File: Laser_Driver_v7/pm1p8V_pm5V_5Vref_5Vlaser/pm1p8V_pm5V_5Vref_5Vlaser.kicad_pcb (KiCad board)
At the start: 2 copper layers, 160 x 100 mm, 103 parts, among them J6 DIN41612_03x32_C_Split, U1 MC7808CTG, U10 LT3042EMSE +14.3V, U13 MC7812CTG, U14 MC7808CTG, U15 LT3045EMSE 5V, U16 LT3045EMSE 5V, U17 MC7808CTG, U18 MC7906CTG, U19 LT3045EMSE 5V, U2 LT3042EMSE +5.5V, U20 LT3094EMSE -5V, U21 OPA192IDBVR, U3 LTC6655BHMS8-5#PBF, U4 MC7812CTG, U5 MC7805CTG, U6 LT3045EMSE 3.3V, U7 LP5907MFX-1.8, U8 TPS7A3901DSCR, U9 LT3094EMSE -14.3V

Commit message: Working towards a full set of pcbs in v7
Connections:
- J6 pad a20: unconnected-(J6A-Pin_a20-Pada20) -> 5Vref
- J6 pad a22: unconnected-(J6A-Pin_a22-Pada22) -> VREF_MID
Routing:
- net +18V: track 269.0 -> 307.0 mm, vias 0 -> 5
- net +5V_LASER: track 112.0 -> 92.9 mm, vias 1 -> 2
- net 5Vref: track 78.4 -> 96.8 mm
- net +5V: track 138.6 -> 147.9 mm, vias 2 -> 4
- net 1V8: track 71.3 -> 77.4 mm, vias 2 -> 4
- net 3V3: track 84.3 -> 90.3 mm, vias 2 -> 4
- net -15V: track 65.4 -> 70.2 mm, vias 2 -> 4
- net -18V: track 226.3 -> 229.8 mm, vias 1 -> 2
- net -5V: track 146.5 -> 147.8 mm, vias 2 -> 3
- net VREF_MID: track 75.2 -> 75.9 mm, vias 1 -> 2
- net Net-(U10-EN/UV): track 33.5 -> 34.1 mm
- net +15V: track 66.1 -> 66.7 mm, vias 1 -> 3
- net GND: track 51.6 -> 51.7 mm, vias 270 -> 245

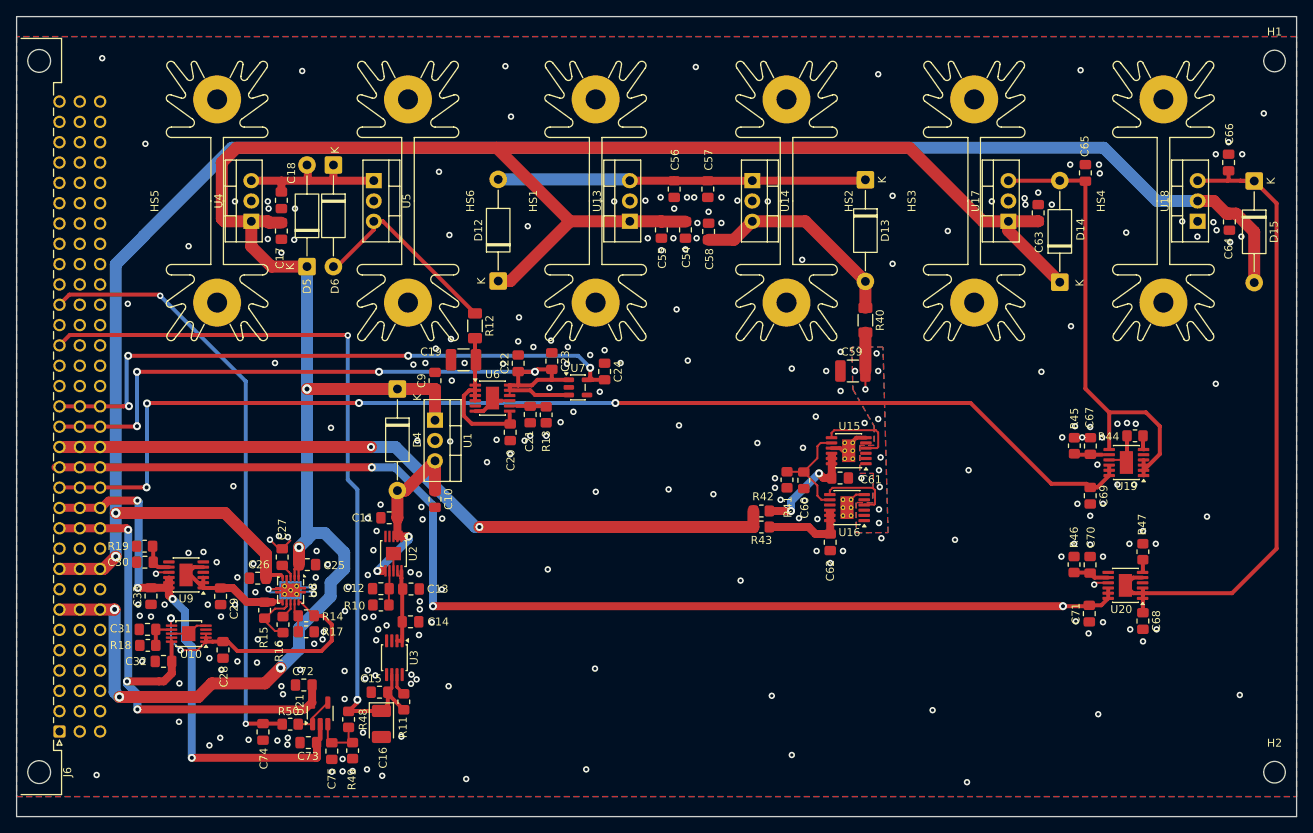
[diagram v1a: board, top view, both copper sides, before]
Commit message: Updates to capacitors for derating.
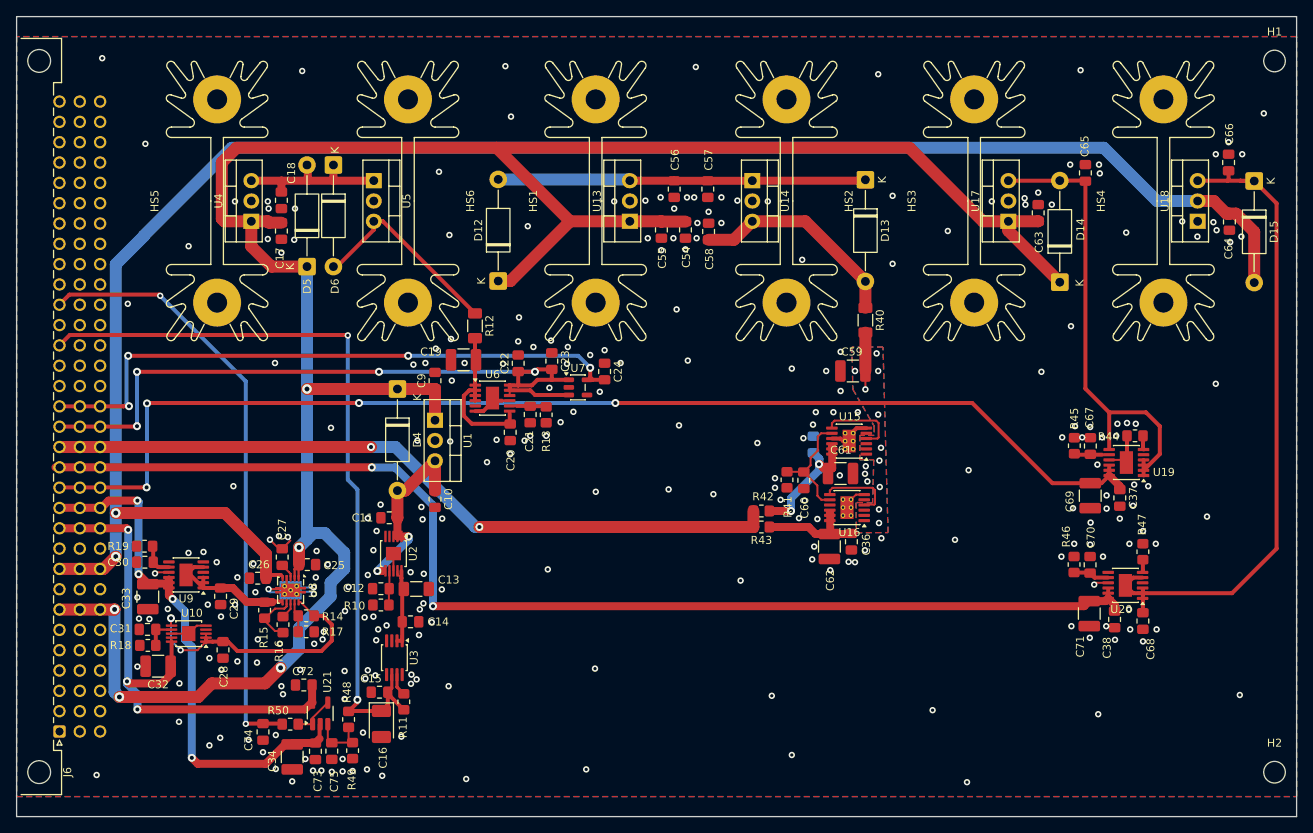
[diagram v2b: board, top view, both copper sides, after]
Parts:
- added C34: 10uF 50V X7R, Capacitor_SMD:C_1210_3225Metric_Pad1.33x2.70mm_HandSolder, F.Cu at (89.5, 137.5)
- added C35: 100nF, Capacitor_SMD:C_0805_2012Metric_Pad1.18x1.45mm_HandSolder, B.Cu at (154.6, 98.5)
- added C36: 100nF, Capacitor_SMD:C_0805_2012Metric_Pad1.18x1.45mm_HandSolder, F.Cu at (159.3, 110.6)
- added C37: 100nF, Capacitor_SMD:C_0805_2012Metric_Pad1.18x1.45mm_HandSolder, F.Cu at (192.9, 105.2)
- added C38: 100nF, Capacitor_SMD:C_0805_2012Metric_Pad1.18x1.45mm_HandSolder, F.Cu at (192.2, 120.3)
- C13: value 4.7uF -> 10uF 25V X7R; footprint Capacitor_SMD:C_0805_2012Metric_Pad1.18x1.45mm_HandSolder -> Capacitor_SMD:C_1206_3216Metric_Pad1.33x1.80mm_HandSolder
- C25, C26: value 10uF -> 4.7uF 50V X7R
- C32, C33: value 10uF -> 10uF 50V X7R; footprint Capacitor_SMD:C_0805_2012Metric_Pad1.18x1.45mm_HandSolder -> Capacitor_SMD:C_1210_3225Metric_Pad1.33x2.70mm_HandSolder
- C54: value 4.7uF -> 4.7uF 50V X7R
- C61, C62, C71: value 10uF -> 22uF 25V X7R; footprint Capacitor_SMD:C_0805_2012Metric_Pad1.18x1.45mm_HandSolder -> Capacitor_SMD:C_1210_3225Metric_Pad1.33x2.70mm_HandSolder
- C69: value 10uF X5R or X7R -> 22uF 25V X7R; footprint Capacitor_SMD:C_0805_2012Metric_Pad1.18x1.45mm_HandSolder -> Capacitor_SMD:C_1210_3225Metric_Pad1.33x2.70mm_HandSolder
- moved C73 1.40 mm to (92.3, 136.8), turned to -90 degrees
- moved U15 1.20 mm to (159.1, 98.1)
- moved C32 0.90 mm to (72.7, 126.2)
- moved C13 0.66 mm to (105.0, 116.5)
- moved C61 0.56 mm to (158.0, 102.1)
- moved C62 0.53 mm to (156.6, 111.2)
- moved C33 0.41 mm to (71.4, 117.5)
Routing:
- net Net-(U15-OUTS): track 13.4 -> 16.4 mm
- net Net-(U16-OUTS): track 10.6 -> 13.4 mm
- net -15V: track 70.2 -> 68.0 mm
- net -5V: track 147.8 -> 149.7 mm, vias 3 -> 2
- net +5V: track 147.9 -> 149.8 mm
- net Net-(U15-SET): track 13.4 -> 14.6 mm
- net GND: vias 245 -> 263

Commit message: minor updates and U for FBG
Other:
- board text added: "pm1p8V v7"
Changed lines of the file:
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@@
 	)
 	(embedded_fonts no)
+	(gr_text "pm1p8V v7"
+		(at 74.925 50.250 0)
+		(layer "B.SilkS")
+		(effects
+			(font
+				(size 1.5 1.5)
+				(thickness 0.25)
+			)
+			(justify mirror)
+		)
+	)
 )
